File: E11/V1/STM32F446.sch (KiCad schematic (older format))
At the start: 37 parts, among them J201 Header_Male_Pin_2.54mm_1X6_,_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, J202 Header_Male_Pin_2.54mm_1X3_,_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, SW201 PTS645SM43SMTR92, SW202 PTS645SM43SMTR92, U201 STM32F446RE

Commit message: most of the parts have been migrated to new board outline
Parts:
- removed C201, C202: 885012007027, Capacitors:C0805, symbol Capacitors:885012007027
- removed R201: RC0805JR-070RL, Resistors:R0805, symbol Resistors:RC0805JR-070RL
- removed XTAL201: ABS25-32.768KHZ-6-T, Crystals:ABS25, symbol Crystals:ABS25-32.768KHZ-6-T
- C203, C207, C210, C212, C213, C214: footprint Capacitors:C0805 -> Capacitors:C0603; symbol Capacitors:885012207098 -> Capacitors:885012206095; Description CAP CER 0.1UF 50V X7R 0805 -> CAP CER 0.1UF 50V X7R 0603; Manufacturer Part Number 885012207098 -> 885012206095; Supplier Part Number 732-8080-1-ND -> 732-8013-2-ND
- C204, C208: footprint Capacitors:C0805 -> Capacitors:C0603; symbol Capacitors:885012107015 -> Capacitors:885012106022; Description CAP CER 1UF 25V X5R 0805 -> CAP CER 1UF 25V X5R 0603; Manufacturer Part Number 885012107015 -> 885012106022; Supplier Part Number 732-7625-1-ND -> 732-7919-2-ND
- C205, C206, C215: footprint Capacitors:C0805 -> Capacitors:C0603; symbol Capacitors:885012007053 -> Capacitors:885012006053; Description CAP CER 22PF 50V C0G/NP0 0805 -> CAP CER 22PF 50V X7R 0603; Manufacturer Part Number 885012007053 -> 885012206077; Supplier Part Number 732-7848-1-ND -> 732-7995-2-ND
- C209: footprint Capacitors:C0805 -> Capacitors:C0603; symbol Capacitors:885012207092 -> Capacitors:885012206089; Description CAP CER 10000PF 50V X7R 0805 -> CAP CER 10nF 50V X7R 0603; Manufacturer Part Number 885012207092 -> 885012206089; Supplier Part Number 732-8074-1-ND -> 732-8007-2-ND
- C211: footprint Capacitors:C0805 -> Capacitors:C0603; symbol Capacitors:885012107018 -> Capacitors:GRT188C81E475KE13D; Description CAP CER 4.7UF 25V X5R 0805 -> CAP CER 4.7UF 25V X6S 0603; Manufacturer Wurth Electronics Inc. -> Murata Electronics; Manufacturer Part Number 885012107018 -> GRT188C81E475KE13D; Supplier Part Number 732-7628-1-ND -> 490-12295-2-ND; Tolerance (%) ±20% -> ±10%
- R202: footprint Resistors:R0805 -> Resistors:R0603; symbol Resistors:RC0805JR-070RL -> Resistors:RC0603FR-07100RL; Description RES SMD 0.0 OHM JUMPER 1/8W 0805 -> RES SMD 100 OHM 1% 1/10W 0603; Manufacturer Part Number RC0805JR-070RL -> RC0603FR-07100RL; Puissance (Watts) 1/8W -> 1/10W; Supplier Part Number 311-0.0ARCT-ND -> 311-100HRTR-ND; Tolerance (%) 0 -> ±5%
- R203, R205, R207: footprint Resistors:R0805 -> Resistors:R0603; symbol Resistors:RC0805JR-074K7L -> Resistors:RC0603JR-074K7L; Description RES SMD 4.7K OHM 5% 1/8W 0805 -> RES SMD 4.7K OHM 5% 1/10W 0603; Manufacturer Part Number RC0805JR-074K7L -> RC0603JR-074K7L; Puissance (Watts) 1/8W -> 1/10W; Supplier Part Number 311-4.7KARCT-ND -> 311-4.7KGRTR-ND
- R204, R206: footprint Resistors:R0805 -> Resistors:R0603; symbol Resistors:RC0805JR-07100RL -> Resistors:RC0603FR-07100RL; Description RES SMD 100 OHM 5% 1/8W 0805 -> RES SMD 100 OHM 1% 1/10W 0603; Manufacturer Part Number RC0805JR-07100RL -> RC0603FR-07100RL; Puissance (Watts) 1/8W -> 1/10W; Supplier Part Number 311-100ARCT-ND -> 311-100HRTR-ND
- R208, R209, R210: footprint Resistors:R0805 -> Resistors:R0603; symbol Resistors:RC0805JR-07470RL -> Resistors:RC0603JR-07470RL; Description RES SMD 470 OHM 5% 1/8W 0805 -> RES SMD 470 OHM 5% 1/10W 0603; Manufacturer Part Number RC0805JR-07470RL -> RC0603JR-07470RL; Puissance (Watts) 1/8W -> 1/10W; Supplier Part Number 311-470ARCT-ND -> 311-470GRTR-ND
- R211: footprint Resistors:R0805 -> Resistors:R0603; symbol Resistors:RC0805JR-071KL -> Resistors:RC0603JR-071KL; Description RES SMD 1K OHM 5% 1/8W 0805 -> RES SMD 1K OHM 5% 1/10W 0603; Manufacturer Part Number RC0805JR-071KL -> RC0603JR-071KL; Puissance (Watts) 1/8W -> 1/10W; Supplier Part Number 311-1.0KARCT-ND -> 311-1.0KGRTR-ND
- R212: footprint Resistors:R0805 -> Resistors:R0603; symbol Resistors:RC0805JR-0710KL -> Resistors:RC0603JR-0710KP; Description RES SMD 10K OHM 5% 1/8W 0805 -> RES SMD 10K OHM 5% 1/10W 0603; Manufacturer Part Number RC0805JR-0710KL -> RC0603JR-0710KP; Puissance (Watts) 1/8W -> 1/10W; Supplier Part Number 311-10KARCT-ND -> YAG1309TR-ND
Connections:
- no-connect marks 5 -> 7
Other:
- note added: "REMOVED"

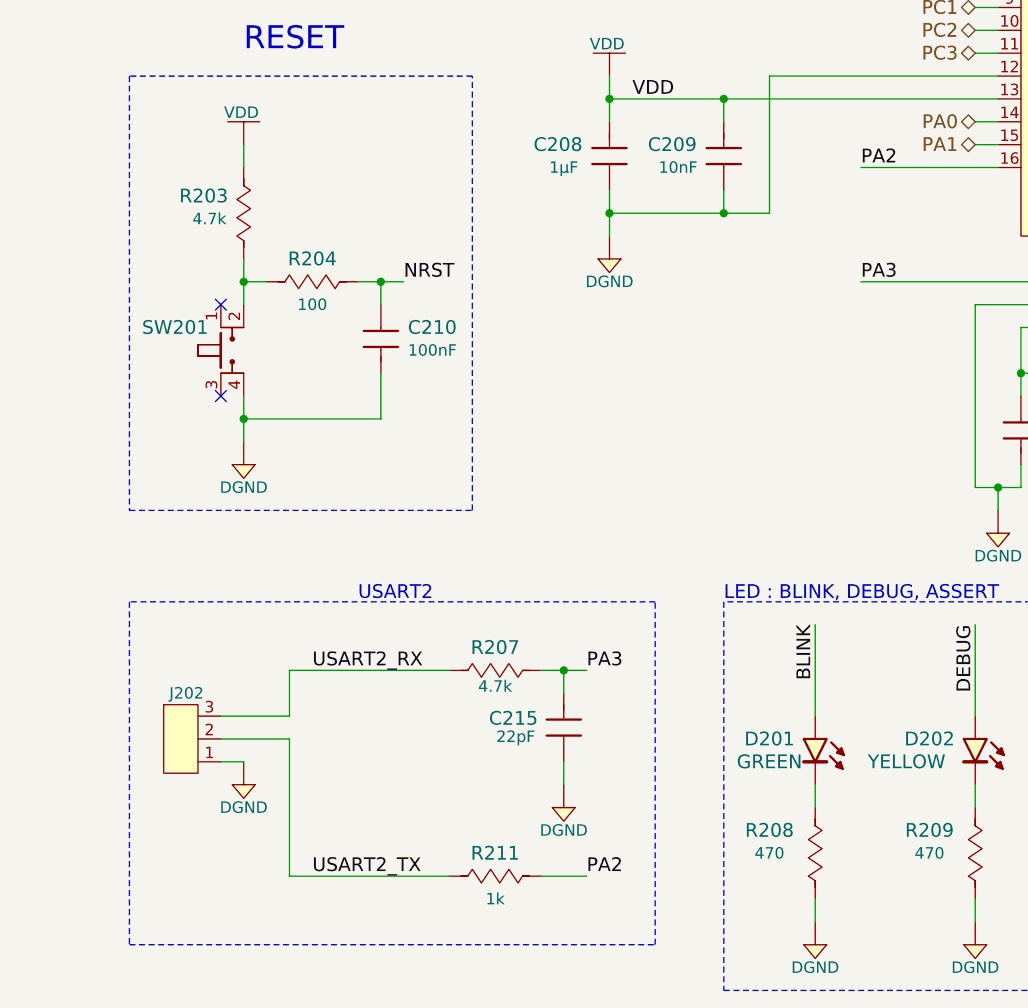
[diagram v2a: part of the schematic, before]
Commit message: initial component placement done
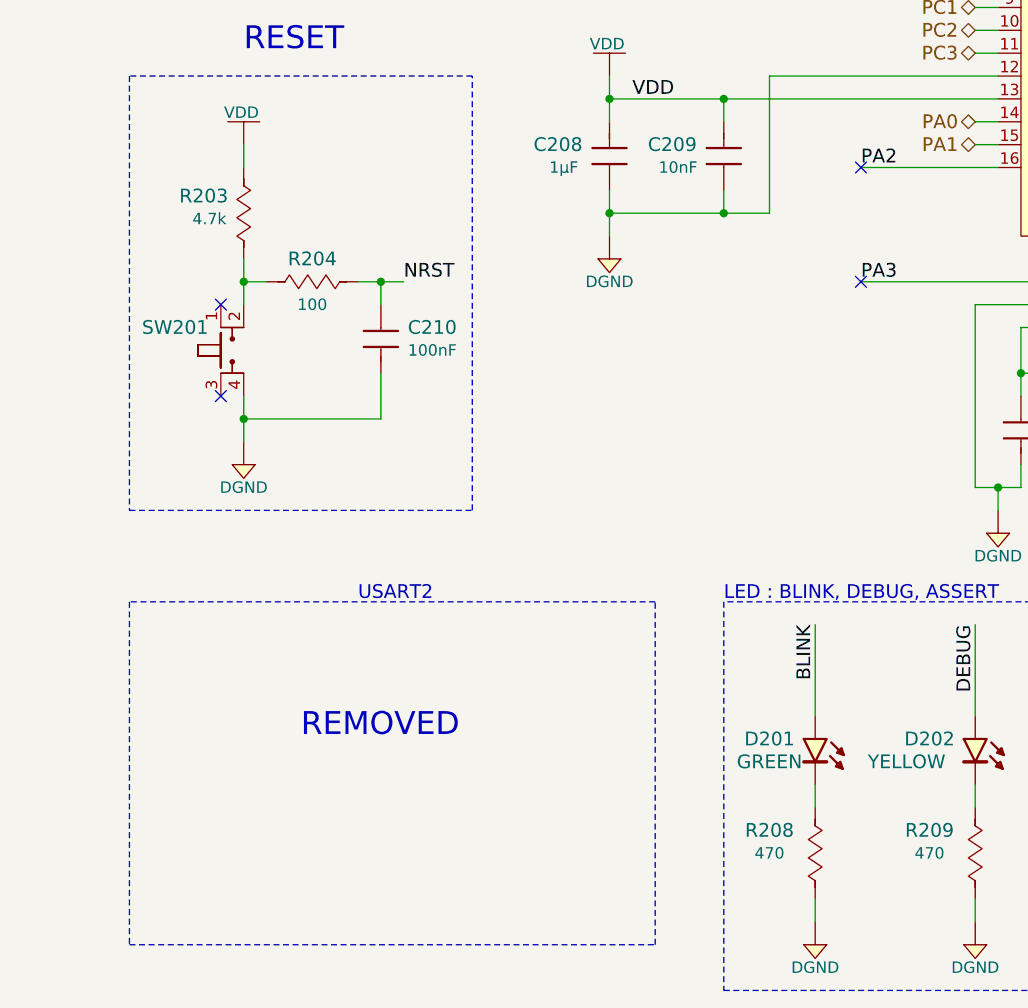
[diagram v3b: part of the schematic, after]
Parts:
- removed C215: 885012007053, Capacitors:C0603, symbol Capacitors:885012006053
- removed J202: Header_Male_Pin_2.54mm_1X3_,_Unshrouded, Connectors:Headers_2.54mm_1X3, symbol Connectors:Header_Male_Pin_2.54mm_1X3_,_Unshrouded
- removed R207: RC0805JR-074K7L, Resistors:R0603, symbol Resistors:RC0603JR-074K7L
- removed R211: RC0805JR-071KL, Resistors:R0603, symbol Resistors:RC0603JR-071KL
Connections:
- no-connect marks 7 -> 9
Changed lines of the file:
@@
 NoConn ~ 900  5400
 NoConn ~ 900  5000
-Text Label 1300 7500 0    60   ~ 0
-USART2_TX
 Text Label 3700 4900 0    60   ~ 0
 PA3
 Wire Wire Line
 	4700 4900 3700 4900
-$Comp
-L Resistors:RC0603JR-074K7L R207
-U 1 1 58F95EAF
-P 2100 6600
-F 0 "R207" H 2100 6700 60  0000 C CNN
-F 1 "RC0805JR-074K7L" H 2100 6300 50  0001 C CNN
-F 2 "Resistors:R0603" H 2100 5700 30  0001 C CNN
-F 3 "https://www.yageo.com/upload/media/product/productsearch/datasheet/rchip/PYu-RC_Group_51_RoHS_L_10.pdf" H 2100 5650 30  0001 C CNN
-F 4 "Digikey" H 2100 6200 60  0001 C CNN "Supplier"
-F 5 "311-4.7KGRTR-ND" H 2100 6100 60  0001 C CNN "Supplier Part Number"
-F 6 "Yageo" H 2100 6000 60  0001 C CNN "Manufacturer"
-F 7 "RC0603JR-074K7L" H 2100 5900 60  0001 C CNN "Manufacturer Part Number"
-F 8 "RES SMD 4.7K OHM 5% 1/10W 0603" H 2100 5800 60  0001 C CNN "Description"
-F 9 "4.7k" H 2100 6530 50  0000 C CNN "Resistance (Ohms)"
-F 10 "±5%" H 2300 6500 50  0001 C CNN "Tolerance (%)"
-F 11 "1/10W" H 2100 6460 50  0001 C CNN "Puissance (Watts)"
-	1    2100 6600
-	1    0    0    -1
-$EndComp
-Text Label 1300 6600 0    60   ~ 0
-USART2_RX
-Wire Wire Line
-	2300 6600 2400 6600
-Wire Wire Line
-	2300 7500 2500 7500
-$Comp
-L Power_Port:DGND #PWR0207
-U 1 1 58F96748
-P 2400 7200
-F 0 "#PWR0207" H 2400 7030 50  0001 C CNN
-F 1 "DGND" H 2400 7100 50  0000 C CNN
-F 2 "" H 2400 7300 60  0000 C CNN
-F 3 "" H 2380 7110 60  0000 C CNN
-	1    2400 7200
-	1    0    0    -1
-$EndComp
-Wire Wire Line
-	2400 7000 2400 7100
 Text Label 3700 4400 0    60   ~ 0
 PA2
-Text Label 2500 7500 0    60   ~ 0
-PA2
-Text Label 2500 6600 0    60   ~ 0
-PA3
-Wire Wire Line
-	1200 6600 1900 6600
-Wire Wire Line
-	1200 7500 1900 7500
-$Comp
-L Resistors:RC0603JR-071KL R211
-U 1 1 58F97B70
-P 2100 7500
-F 0 "R211" H 2100 7600 60  0000 C CNN
-F 1 "RC0805JR-071KL" H 2100 7200 50  0001 C CNN
-F 2 "Resistors:R0603" H 2100 6600 30  0001 C CNN
-F 3 "https://www.yageo.com/upload/media/product/productsearch/datasheet/rchip/PYu-RC_Group_51_RoHS_L_10.pdf" H 2100 6550 30  0001 C CNN
-F 4 "Digikey" H 2100 7100 60  0001 C CNN "Supplier"
-F 5 "311-1.0KGRTR-ND" H 2100 7000 60  0001 C CNN "Supplier Part Number"
-F 6 "Yageo" H 2100 6900 60  0001 C CNN "Manufacturer"
-F 7 "RC0603JR-071KL" H 2100 6800 60  0001 C CNN "Manufacturer Part Number"
-F 8 "RES SMD 1K OHM 5% 1/10W 0603" H 2100 6700 60  0001 C CNN "Description"
-F 9 "1k" H 2100 7400 50  0000 C CNN "Resistance (Ohms)"
-F 10 "±5%" H 2510 7420 50  0001 C CNN "Tolerance (%)"
-F 11 "1/10W" H 2100 7360 50  0001 C CNN "Puissance (Watts)"
-	1    2100 7500
-	1    0    0    -1
-$EndComp
 $Comp
 L Diodes:150080VS75000 D201
@@
 Text Notes 3100 6300 0    60   ~ 0
 LED : BLINK, DEBUG, ASSERT
-Wire Wire Line
-	900  7000 1000 7000
-$Comp
-L Power_Port:DGND #PWR0204
-U 1 1 58F912A3
-P 1000 7100
-F 0 "#PWR0204" H 1000 6930 50  0001 C CNN
-F 1 "DGND" H 1000 7000 50  0000 C CNN
-F 2 "" H 1000 7200 60  0000 C CNN
-F 3 "" H 980 7010 60  0000 C CNN
-	1    1000 7100
-	1    0    0    -1
-$EndComp
 Wire Notes Line
 	500  6300 500  7800
@@
 Text Notes 1500 6300 0    60   ~ 0
 USART2
-$Comp
-L Connectors:Header_Male_Pin_2.54mm_1X3_,_Unshrouded J202
-U 1 1 58F8E26A
-P 800 7000
-F 0 "J202" H 750 7300 50  0000 C CNN
-F 1 "Header_Male_Pin_2.54mm_1X3_,_Unshrouded" H 800 6680 50  0001 C CNN
-F 2 "Connectors:Headers_2.54mm_1X3" H 800 6090 30  0001 C CNN
-F 3 "D" H 800 6040 30  0001 C CNN
-F 4 "Ebay" H 800 6490 60  0001 C CNN "Supplier"
-F 5 "Pin Male Single Row Pin Header Strip" H 800 6590 60  0001 C CNN "Supplier Part Number"
-F 6 "Manufacturer" H 800 6390 60  0001 C CNN "Manufacturer"
-F 7 "Manufacturer Part Number" H 800 6290 60  0001 C CNN "Manufacturer Part Number"
-F 8 "Pin Male Single Row Pin Header Strip" H 800 6190 60  0001 C CNN "Description"
-	1    800  7000
-	1    0    0    -1
-$EndComp
 Connection ~ 7400 2800
 Text Label 7100 3200 0    60   ~ 0
@@
 	1    0    0    -1
 $EndComp
-Wire Wire Line
-	1200 7500 1200 6900
-Wire Wire Line
-	1200 6900 900  6900
-Wire Wire Line
-	900  6800 1200 6800
-Wire Wire Line
-	1200 6800 1200 6600
 $Comp
 L Capacitors:885012106022 C204
@@
 NRST
 Wire Wire Line
-	2400 6700 2400 6600
-Connection ~ 2400 6600
-$Comp
-L Capacitors:885012006053 C215
-U 1 1 590A2D9C
-P 2400 6800
-F 0 "C215" V 2390 7020 60  0000 C CNN
-F 1 "885012007053" H 2350 6450 60  0001 C CNN
-F 2 "Capacitors:C0603" H 2350 5850 60  0001 C CNN
-F 3 "https://www.we-online.de/katalog/datasheet/885012006053.pdf" H 2350 5750 60  0001 C CNN
-F 4 "Digikey" H 2350 6350 60  0001 C CNN "Supplier"
-F 5 "732-7995-2-ND" H 2350 6250 60  0001 C CNN "Supplier Part Number"
-F 6 "Wurth Electronics Inc." H 2350 6150 60  0001 C CNN "Manufacturer"
-F 7 "885012206077" H 2350 6050 60  0001 C CNN "Manufacturer Part Number"
-F 8 "CAP CER 22PF 50V X7R 0603" H 2350 5950 60  0001 C CNN "Description"
-F 9 "22pF" V 2310 7010 50  0000 C CNN "Capacitance (Farad)"
-F 10 "±5%" H 2610 6680 50  0001 C CNN "Tolerance (%)"
-F 11 "50V" H 2350 6610 50  0001 C CNN "Voltage Rated (Volt)"
-	1    2400 6800
-	0    -1   -1   0
-$EndComp
-Wire Wire Line
 	3100 4100 4300 4100
 Wire Wire Line
@@
 Wire Wire Line
 	4200 2900 4300 2900
-Wire Wire Line
-	2400 6600 2500 6600
 $Comp
 L Resistors:RC0603JR-0710KP R212
@@
 NoConn ~ 4300 3100
 NoConn ~ 4300 3200
+Text Notes 1250 6900 0    100  ~ 0
+REMOVED
+NoConn ~ 3700 4900
+NoConn ~ 3700 4400
 $EndSCHEMATC
